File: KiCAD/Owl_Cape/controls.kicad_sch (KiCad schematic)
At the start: 3 parts, among them J17 OLED, SW1 Enter BTN, SW2 Down BTN

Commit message: started routing cu
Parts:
- added J18, J19: 8P8C_LED_Shielded, Connector_RJ:RJ45_BEL_SS74301-00x_Vertical, symbol Connector:8P8C_LED_Shielded
- added R40, R41: (no value), symbol Device:R_Small
- added U3: TZT_Original_0.96_inch_oled_IIC_Serial_OLED_Displ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, Stuart_BESPOKE:TZT_0.96inch_OLED, symbol Stuarts_BESPOKE:TZT_Original_0.96_inch_oled_IIC_Serial_OLED_Display_Module_128X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
- added U4: (no value), symbol Interface_Ethernet:LAN7500-ABJZ
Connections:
- net +3V3: now also U4.1 (TDI), U4.15 (VDD33A), U4.19 (VDDVARIO), U4.2 (TCK), U4.24 (VDDVARIO), U4.3 (TMS), U4.37 (VDDVARIO), U4.39 (TEST), U4.7 (VDDVARIO)
- net GND: now also J18.11, J18.9, J18.SH, J19.11, J19.9, J19.SH, R40.1, R41.1, U4.57 (GND)
- new net: R40.2, U4.16 (USBRBIAS)
- new net: U4.11 (VDD12CORE), U4.20 (VDD12CORE), U4.23 (VDD12CORE), U4.30 (VDD12CORE), U4.36 (VDD12CORE), U4.8 (VDD12CORE)
- new net: J18.10, U4.31 (GPIO0)
- new net: J18.12, U4.32 (GPIO1)
- new net: U4.45 (VDD12A), U4.48 (VDD12A), U4.53 (VDD12A), U4.56 (VDD12A)
- new net: R41.2, U4.41 (ETHRBIAS)
- new net: J18.1, U4.43 (TR0N)
- new net: J18.2, U4.44 (TR0P)
- new net: J18.3, U4.46 (TR1N)
- new net: J18.4, U4.47 (TR1P)
- new net: J18.5, U4.51 (TR2N)
- new net: J18.6, U4.52 (TR2P)
- new net: J18.7, U4.54 (TR3N)
- new net: J18.8, U4.55 (TR3P)
- new net USBDM: U4.12 (USBDM)
- new net USBDP: U4.13 (USBDP)
- no-connect marks 0 -> 15
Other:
- moved on the sheet: J17

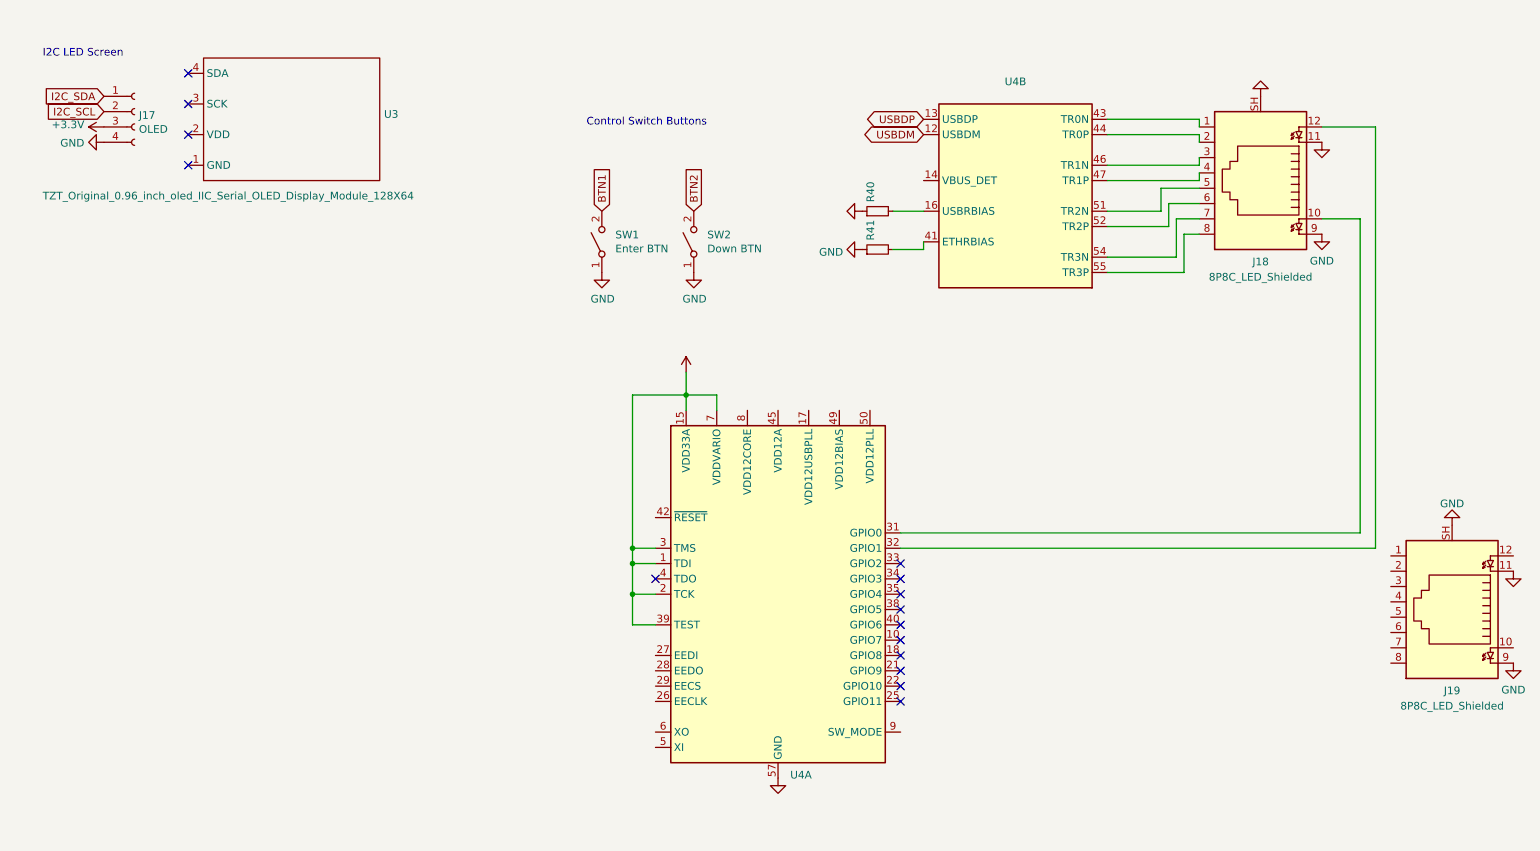
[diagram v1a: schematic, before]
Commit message: swap chips to better speed / layout
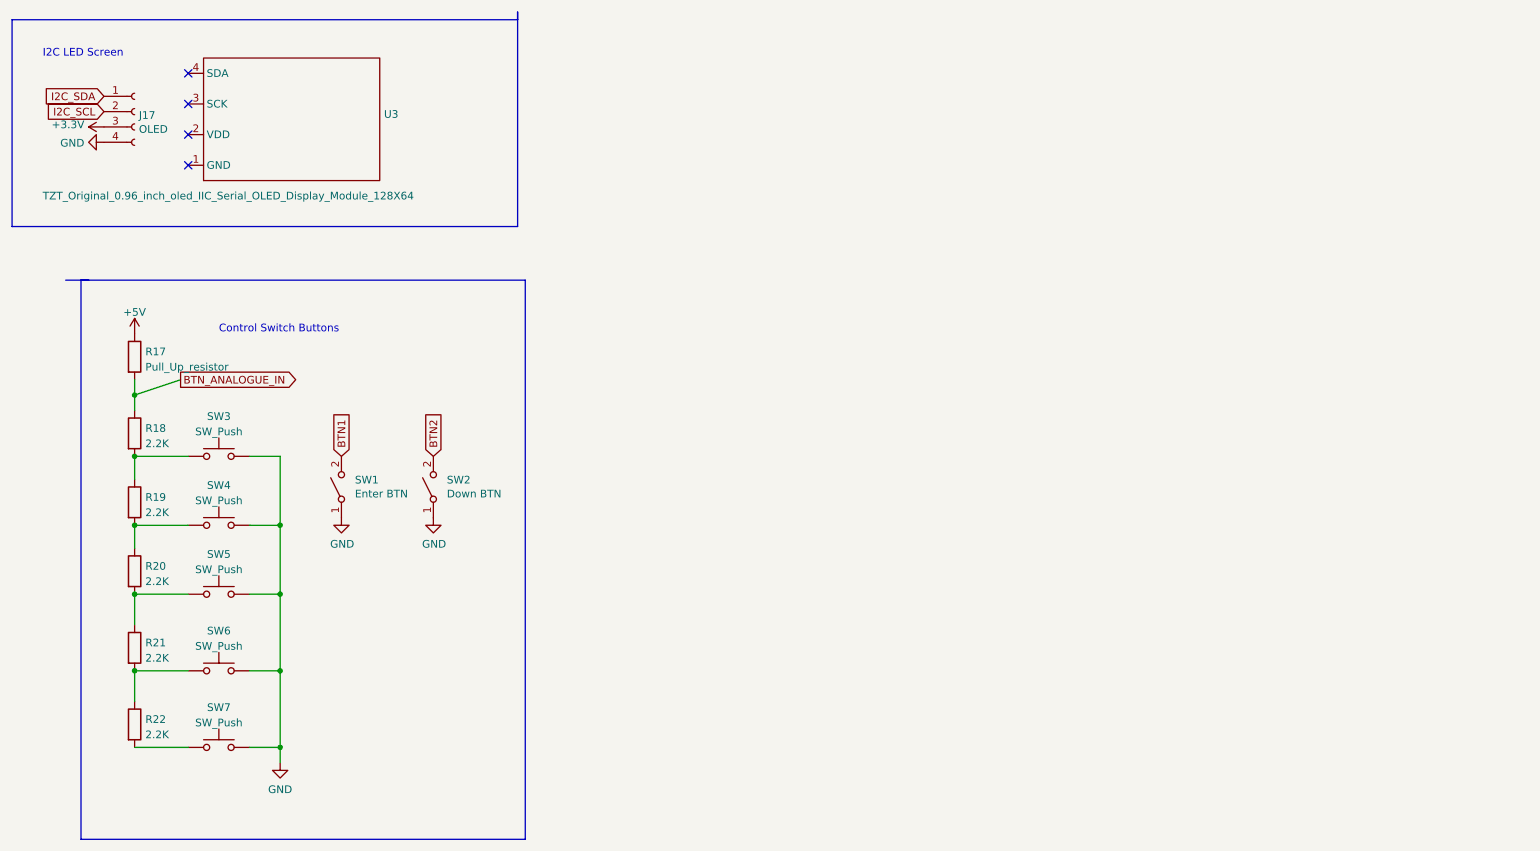
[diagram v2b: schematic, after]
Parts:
- removed J18, J19: 8P8C_LED_Shielded, Connector_RJ:RJ45_BEL_SS74301-00x_Vertical, symbol Connector:8P8C_LED_Shielded
- removed R40, R41: (no value), symbol Device:R_Small
- removed U4: (no value), symbol Interface_Ethernet:LAN7500-ABJZ
- added R17: Pull_Up_resistor, symbol Device:R
- added R18, R19, R20, R21, R22: 2.2K, symbol Device:R
- added SW3, SW4, SW5, SW6, SW7: SW_Push, symbol Switch:SW_Push
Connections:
- net GND: now also SW3.2, SW4.2, SW5.2, SW6.2, SW7.2
- new net: R19.2, R20.1, SW4.1
- new net: R20.2, R21.1, SW5.1
- new net: R21.2, R22.1, SW6.1
- new net: R22.2, SW7.1
- new net: R18.2, R19.1, SW3.1
- new net +5V: R17.1
- new net BTN_ANALOGUE_IN: R17.2, R18.1
- no-connect marks 15 -> 4
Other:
- moved on the sheet: SW1, SW2

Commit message: major update to layout
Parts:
- removed SW2: Down BTN, Button_Switch_THT:SW_PUSH_6mm, symbol Switch:SW_SPST
- J21: renamed from SW1; value Enter BTN -> (none); footprint Button_Switch_THT:SW_PUSH_6mm -> (none); symbol Switch:SW_SPST -> Connector:Conn_01x03_Male
- R17, R18, R19, R20, R21, R22: footprint (none) -> Resistor_SMD:R_0805_2012Metric
- SW3: value SW_Push -> SW_UP; footprint (none) -> Button_Switch_THT:SW_PUSH_6mm
- SW4: value SW_Push -> SW_RIGHT; footprint (none) -> Button_Switch_THT:SW_PUSH_6mm
- SW5: value SW_Push -> SW_DOWN; footprint (none) -> Button_Switch_THT:SW_PUSH_6mm
- SW6: value SW_Push -> SW_LEFT; footprint (none) -> Button_Switch_THT:SW_PUSH_6mm
- SW7: value SW_Push -> SW_ENTER; footprint (none) -> Button_Switch_THT:SW_PUSH_6mm
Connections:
- net BTN1: now also J21.1 (Pin_1); no longer J21.2 (B)
- net GND: now also J21.2 (Pin_2), J21.3 (Pin_3); no longer J21.1 (A)
- net BTN_ANALOGUE_IN renamed BTN_ARRAY_ANALOGUE_IN
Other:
- note added: "GENERAL GPIO Trigger Jumper"
- company: (none) -> OnlineDynamic
- title: (none) -> The Owl - RPI Cape 16ch Pixel Controller

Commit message: formatting fix
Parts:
- J21: value (none) -> GPIO TRG; footprint (none) -> Connector_JST:JST_XH_B3B-XH-A_1x03_P2.50mm_Vertical
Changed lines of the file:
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@@
       (effects (font (size 1.27 1.27)) (justify right))
     )
-    (property "Value" "" (id 1) (at 109.5248 76.835 90)
+    (property "Value" "GPIO TRG" (id 1) (at 109.5248 76.835 90)
       (effects (font (size 1.27 1.27)) (justify right))
     )
-    (property "Footprint" "" (id 2) (at 111.76 77.978 0)
+    (property "Footprint" "Connector_JST:JST_XH_B3B-XH-A_1x03_P2.50mm_Vertical" (id 2) (at 111.76 77.978 0)
       (effects (font (size 1.27 1.27)) hide)
     )
